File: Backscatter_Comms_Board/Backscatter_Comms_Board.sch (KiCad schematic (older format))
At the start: 49 parts, among them J1 SPK_IN, J2 Conn_01x09, J3 Conn_01x02, M1 BF1101WR, M2 BF1101WR, T1 SP-48, U1 ADG919BRMZ, U2 ADG841YKSZ-REEL7, U3 NCS2200SQ2T2G

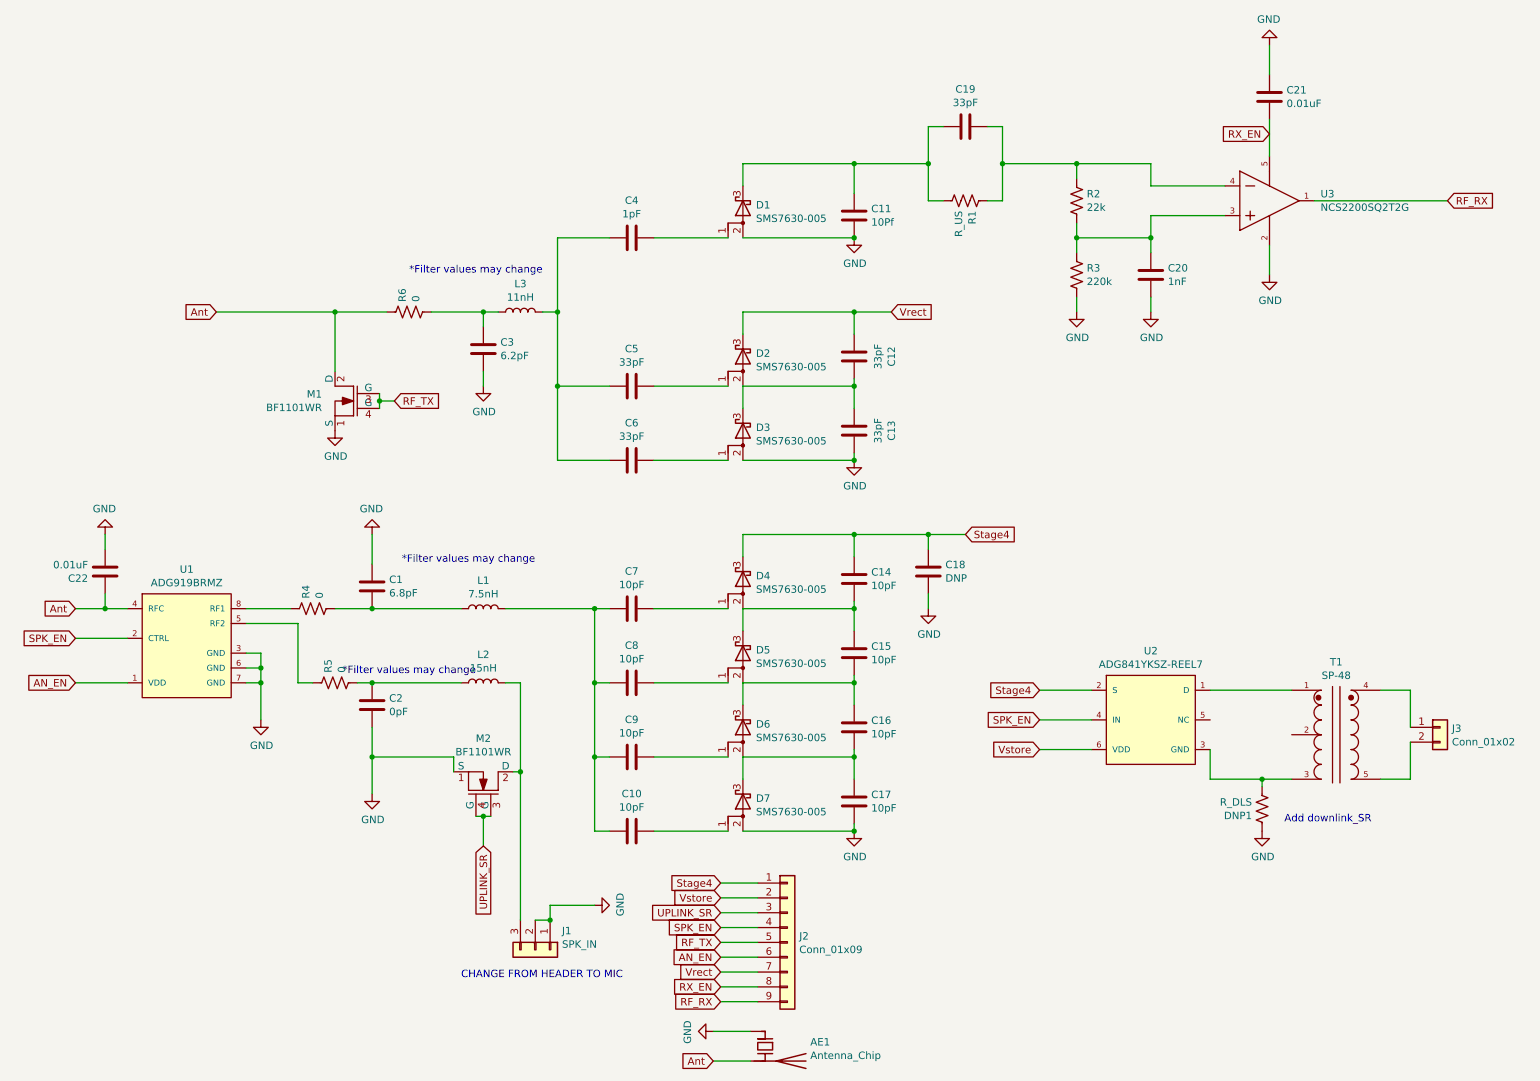
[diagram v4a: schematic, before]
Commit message: Small fixes final
fixed nmos enclosure(again) and added better text
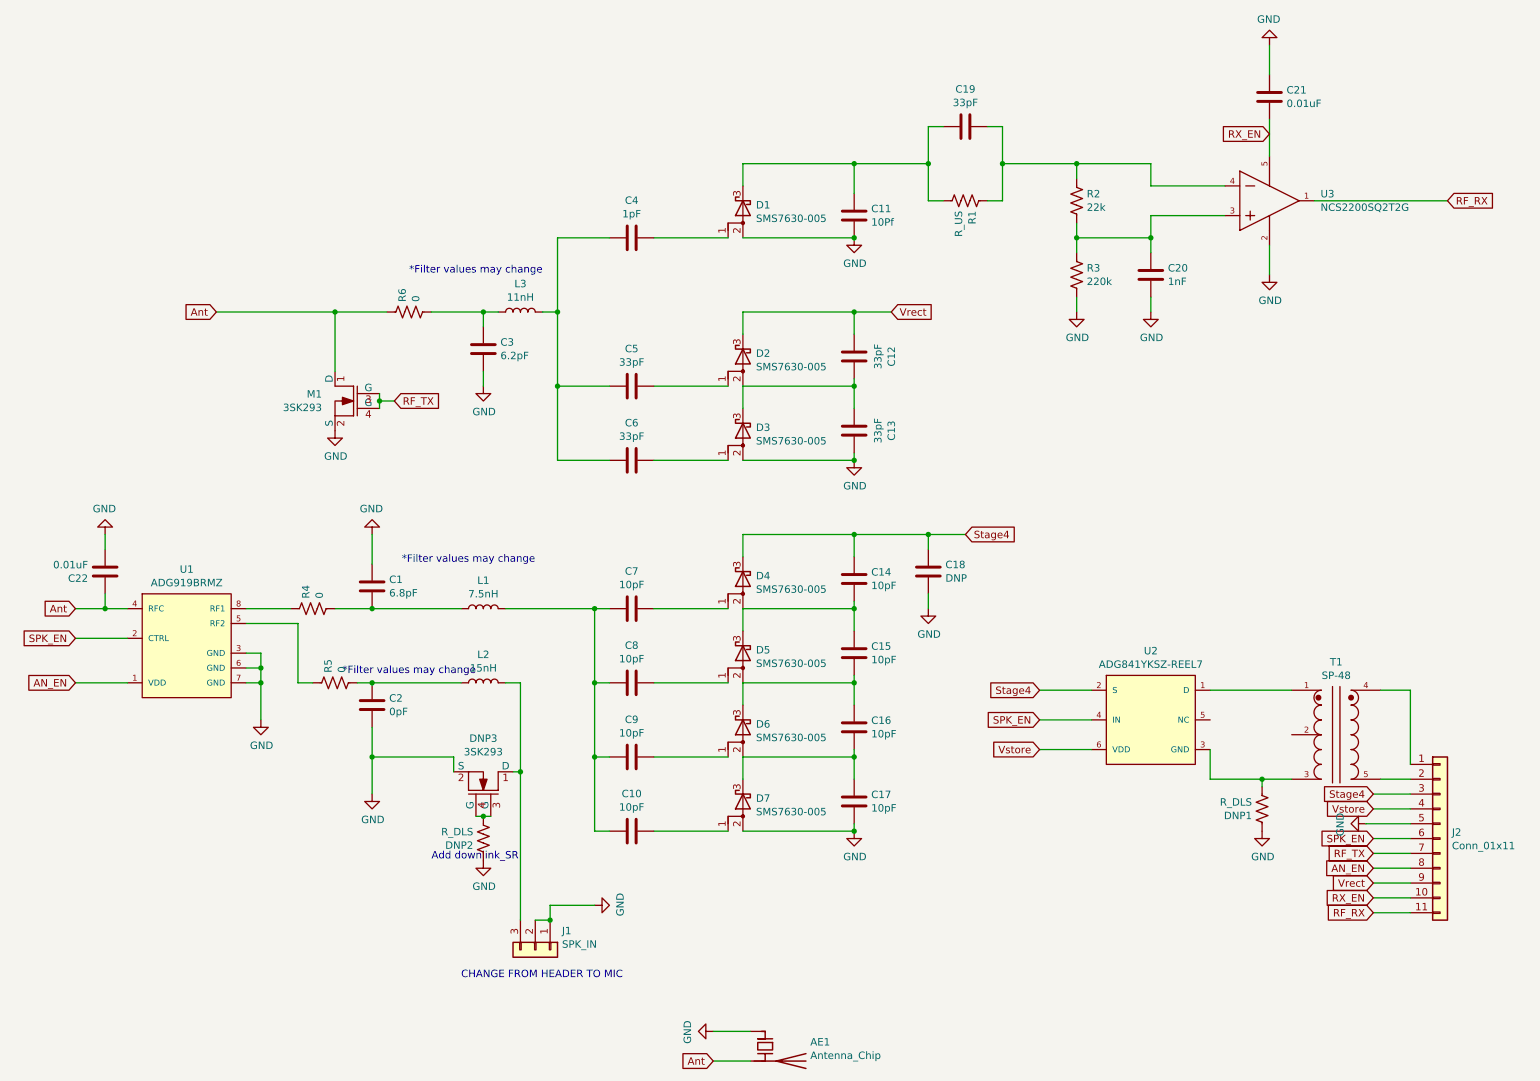
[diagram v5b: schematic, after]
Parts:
- removed J2: Conn_01x09, Connector_PinHeader_2.54mm:PinHeader_1x09_P2.54mm_Vertical, symbol Connector_Generic:Conn_01x09
- removed J3: Conn_01x02, Connector_PinHeader_2.54mm:PinHeader_1x02_P2.54mm_Vertical, symbol Connector_Generic:Conn_01x02
- removed M1, M2: BF1101WR, Local Components:BF1101WR, symbol ADG919:BF1101WR
- added DNP2: R_DLS, Resistor_SMD:R_0402_1005Metric_Pad0.72x0.64mm_HandSolder, symbol Device:R_US
- added DNP3, M1: 3SK293, Local Components:3SK293, symbol ADG919:3SK293
- added J2: Conn_01x11, Connector_PinHeader_2.54mm:PinHeader_1x11_P2.54mm_Vertical, symbol Connector_Generic:Conn_01x11
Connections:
- net AN_EN: now also J2.8 (Pin_8)
- net Ant: now also M1.1 (D)
- net GND: now also DNP2.1, DNP3.2 (S), J2.5 (Pin_5), M1.2 (S)
- net RF_RX: now also J2.11 (Pin_11)
- net RF_TX: now also J2.7 (Pin_7), M1.3 (G), M1.4 (G)
- net RX_EN: now also J2.10 (Pin_10)
- net SPK_EN: now also J2.6 (Pin_6)
- net Stage4: now also J2.3 (Pin_3)
- net Vrect: now also J2.9 (Pin_9)
- net Vstore: now also J2.4 (Pin_4)
- net at J1.3 (Pin_3), L2.2: now also DNP3.1 (D)
- net at T1.4: now also J2.1 (Pin_1)
- net at T1.5: now also J2.2 (Pin_2)
- new net: DNP2.2, DNP3.3 (G), DNP3.4 (G)
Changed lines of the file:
@@
 Wire Wire Line
 	3500 5000 4100 5000
-Wire Wire Line
-	4250 5900 4250 6100
 $Comp
 L Device:C C8
@@
 Text GLabel 10750 1750 2    50   Input ~ 0
 RF_RX
-Text GLabel 4250 6100 3    50   Input ~ 0
-UPLINK_SR
 Connection ~ 6750 3500
 $Comp
@@
 $EndComp
 Wire Wire Line
-	6100 6350 5850 6350
-Wire Wire Line
-	6100 6950 5850 6950
-Wire Wire Line
-	6100 7150 5850 7150
-Wire Wire Line
-	6100 6550 5850 6550
-Text GLabel 5850 6350 0    50   Input ~ 0
+	10500 5750 10250 5750
+Wire Wire Line
+	10500 6350 10250 6350
+Wire Wire Line
+	10500 6550 10250 6550
+Text GLabel 10250 5750 0    50   Input ~ 0
 Stage4
-Text GLabel 5850 7150 0    50   Input ~ 0
+Text GLabel 10250 6550 0    50   Input ~ 0
 RF_RX
 Text GLabel 7500 4000 2    50   Input ~ 0
@@
 Wire Wire Line
 	6750 2500 7000 2500
-Text GLabel 5850 6850 0    50   Input ~ 0
+Text GLabel 10250 6250 0    50   Input ~ 0
 AN_EN
 Text GLabel 5800 7550 0    50   Input ~ 0
@@
 	10300 5650 10500 5650
 $Comp
-L Connector_Generic:Conn_01x02 J3
-U 1 1 6103D8DC
-P 10700 5300
-F 0 "J3" H 10780 5292 50  0000 L CNN
-F 1 "Conn_01x02" H 10780 5201 50  0000 L CNN
-F 2 "Connector_PinHeader_2.54mm:PinHeader_1x02_P2.54mm_Vertical" H 10700 5300 50  0001 C CNN
-F 3 "~" H 10700 5300 50  0001 C CNN
-	1    10700 5300
-	1    0    0    -1
-$EndComp
-Wire Wire Line
-	10300 5050 10500 5050
-Wire Wire Line
-	10500 5050 10500 5300
-Wire Wire Line
-	10500 5400 10500 5650
-$Comp
 L power:GND #PWR09
 U 1 1 610492B0
@@
 $EndComp
 Connection ~ 6750 6000
-Text GLabel 5850 6550 0    50   Input ~ 0
-UPLINK_SR
 $Comp
 L power:GND #PWR013
@@
 	1    0    0    -1
 $EndComp
-Text GLabel 5850 6950 0    50   Input ~ 0
+Text GLabel 10250 6350 0    50   Input ~ 0
 Vrect
 $Comp
@@
 	-1   0    0    1
 $EndComp
-Text GLabel 5850 6750 0    50   Input ~ 0
+Text GLabel 10250 6150 0    50   Input ~ 0
 RF_TX
 Text GLabel 9550 1300 0    50   Input ~ 0
@@
 Wire Wire Line
 	1700 4500 1500 4500
-Text GLabel 5850 6450 0    50   Input ~ 0
+Text GLabel 10250 5850 0    50   Input ~ 0
 Vstore
 Wire Wire Line
-	5850 6450 6100 6450
-$Comp
-L Connector_Generic:Conn_01x09 J2
-U 1 1 60F82694
-P 6300 6750
-F 0 "J2" H 6380 6792 50  0000 L CNN
-F 1 "Conn_01x09" H 6380 6701 50  0000 L CNN
-F 2 "Connector_PinHeader_2.54mm:PinHeader_1x09_P2.54mm_Vertical" H 6300 6750 50  0001 C CNN
-F 3 "~" H 6300 6750 50  0001 C CNN
-	1    6300 6750
-	1    0    0    -1
-$EndComp
+	10250 5850 10500 5850
 $Comp
 L Device:R_US R6
@@
 Wire Wire Line
 	3100 5000 3000 5000
-Text Notes 9650 5950 0    50   ~ 0
-Add downlink_SR\n
-Wire Wire Line
-	6100 6650 5850 6650
-Text GLabel 5850 6650 0    50   Input ~ 0
+Wire Wire Line
+	10500 6050 10250 6050
+Text GLabel 10250 6050 0    50   Input ~ 0
 SPK_EN
 Wire Wire Line
-	5850 7050 6100 7050
-Text GLabel 5850 7050 0    50   Input ~ 0
+	10250 6450 10500 6450
+Text GLabel 10250 6450 0    50   Input ~ 0
 RX_EN
-$Comp
-L ADG919:BF1101WR M1
-U 1 1 6104D965
-P 3350 3100
-F 0 "M1" H 3538 3146 50  0000 L CNN
-F 1 "BF1101WR" H 3538 3055 50  0000 L CNN
-F 2 "Local Components:BF1101WR" H 3325 3100 50  0001 C CNN
-F 3 "~" H 3325 3100 50  0001 C CNN
-	1    3350 3100
-	-1   0    0    -1
-$EndComp
 $Comp
 L power:GND #PWR02
@@
 	3550 3100 3550 3150
 Connection ~ 3550 3100
-$Comp
-L ADG919:BF1101WR M2
-U 1 1 6107F5AB
-P 4250 5700
-F 0 "M2" V 4575 5700 50  0000 C CNN
-F 1 "BF1101WR" V 4484 5700 50  0000 C CNN
-F 2 "Local Components:BF1101WR" H 4225 5700 50  0001 C CNN
-F 3 "~" H 4225 5700 50  0001 C CNN
-	1    4250 5700
-	0    1    -1   0
-$EndComp
-Wire Wire Line
-	4300 5900 4250 5900
-Connection ~ 4250 5900
-Wire Wire Line
-	4250 5900 4200 5900
-Wire Wire Line
-	6100 6750 5850 6750
-Wire Wire Line
-	5850 6850 6100 6850
+Wire Wire Line
+	10500 6150 10250 6150
+Wire Wire Line
+	10250 6250 10500 6250
 Wire Wire Line
 	9150 5650 9500 5650
@@
 Wire Wire Line
 	9500 5650 9700 5650
+$Comp
+L power:GND #PWR0103
+U 1 1 61191A72
+P 4250 6200
+F 0 "#PWR0103" H 4250 5950 50  0001 C CNN
+F 1 "GND" H 4255 6027 50  0000 C CNN
+F 2 "" H 4250 6200 50  0001 C CNN
+F 3 "" H 4250 6200 50  0001 C CNN
+	1    4250 6200
+	1    0    0    -1
+$EndComp
+Text Notes 3900 6200 0    50   ~ 0
+Add downlink_SR\n
+$Comp
+L Device:R_US DNP2
+U 1 1 61191A79
+P 4250 6050
+F 0 "DNP2" H 4318 6096 50  0000 L CNN
+F 1 "R_DLS" H 4318 6005 50  0000 L CNN
+F 2 "Resistor_SMD:R_0402_1005Metric_Pad0.72x0.64mm_HandSolder" V 4290 6040 50  0001 C CNN
+F 3 "~" H 4250 6050 50  0001 C CNN
+	1    4250 6050
+	-1   0    0    1
+$EndComp
+Wire Wire Line
+	4200 5900 4250 5900
+Connection ~ 4250 5900
+Wire Wire Line
+	4250 5900 4300 5900
+$Comp
+L ADG919:3SK293 M1
+U 1 1 611C441C
+P 3350 3100
+F 0 "M1" H 3538 3146 50  0000 L CNN
+F 1 "3SK293" H 3538 3055 50  0000 L CNN
+F 2 "Local Components:3SK293" H 3325 3100 50  0001 C CNN
+F 3 "~" H 3325 3100 50  0001 C CNN
+	1    3350 3100
+	-1   0    0    -1
+$EndComp
+$Comp
+L ADG919:3SK293 DNP3
+U 1 1 611D3BD0
+P 4250 5700
+F 0 "DNP3" V 4575 5700 50  0000 C CNN
+F 1 "3SK293" V 4484 5700 50  0000 C CNN
+F 2 "Local Components:3SK293" H 4225 5700 50  0001 C CNN
+F 3 "~" H 4225 5700 50  0001 C CNN
+	1    4250 5700
+	0    1    -1   0
+$EndComp
+$Comp
+L power:GND #PWR0104
+U 1 1 611E9FE5
+P 10200 5950
+F 0 "#PWR0104" H 10200 5700 50  0001 C CNN
+F 1 "GND" H 10205 5777 50  0000 C CNN
+F 2 "" H 10200 5950 50  0001 C CNN
+F 3 "" H 10200 5950 50  0001 C CNN
+	1    10200 5950
+	0    1    1    0
+$EndComp
+Wire Wire Line
+	10500 5950 10200 5950
+$Comp
+L Connector_Generic:Conn_01x11 J2
+U 1 1 61200553
+P 10700 6050
+F 0 "J2" H 10780 6092 50  0000 L CNN
+F 1 "Conn_01x11" H 10780 6001 50  0000 L CNN
+F 2 "Connector_PinHeader_2.54mm:PinHeader_1x11_P2.54mm_Vertical" H 10700 6050 50  0001 C CNN
+F 3 "~" H 10700 6050 50  0001 C CNN
+	1    10700 6050
+	1    0    0    -1
+$EndComp
+Wire Wire Line
+	10300 5050 10500 5050
+Wire Wire Line
+	10500 5050 10500 5550
 $EndSCHEMATC

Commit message: Final v1 backscatter board
Sending to oshpark right after I push!
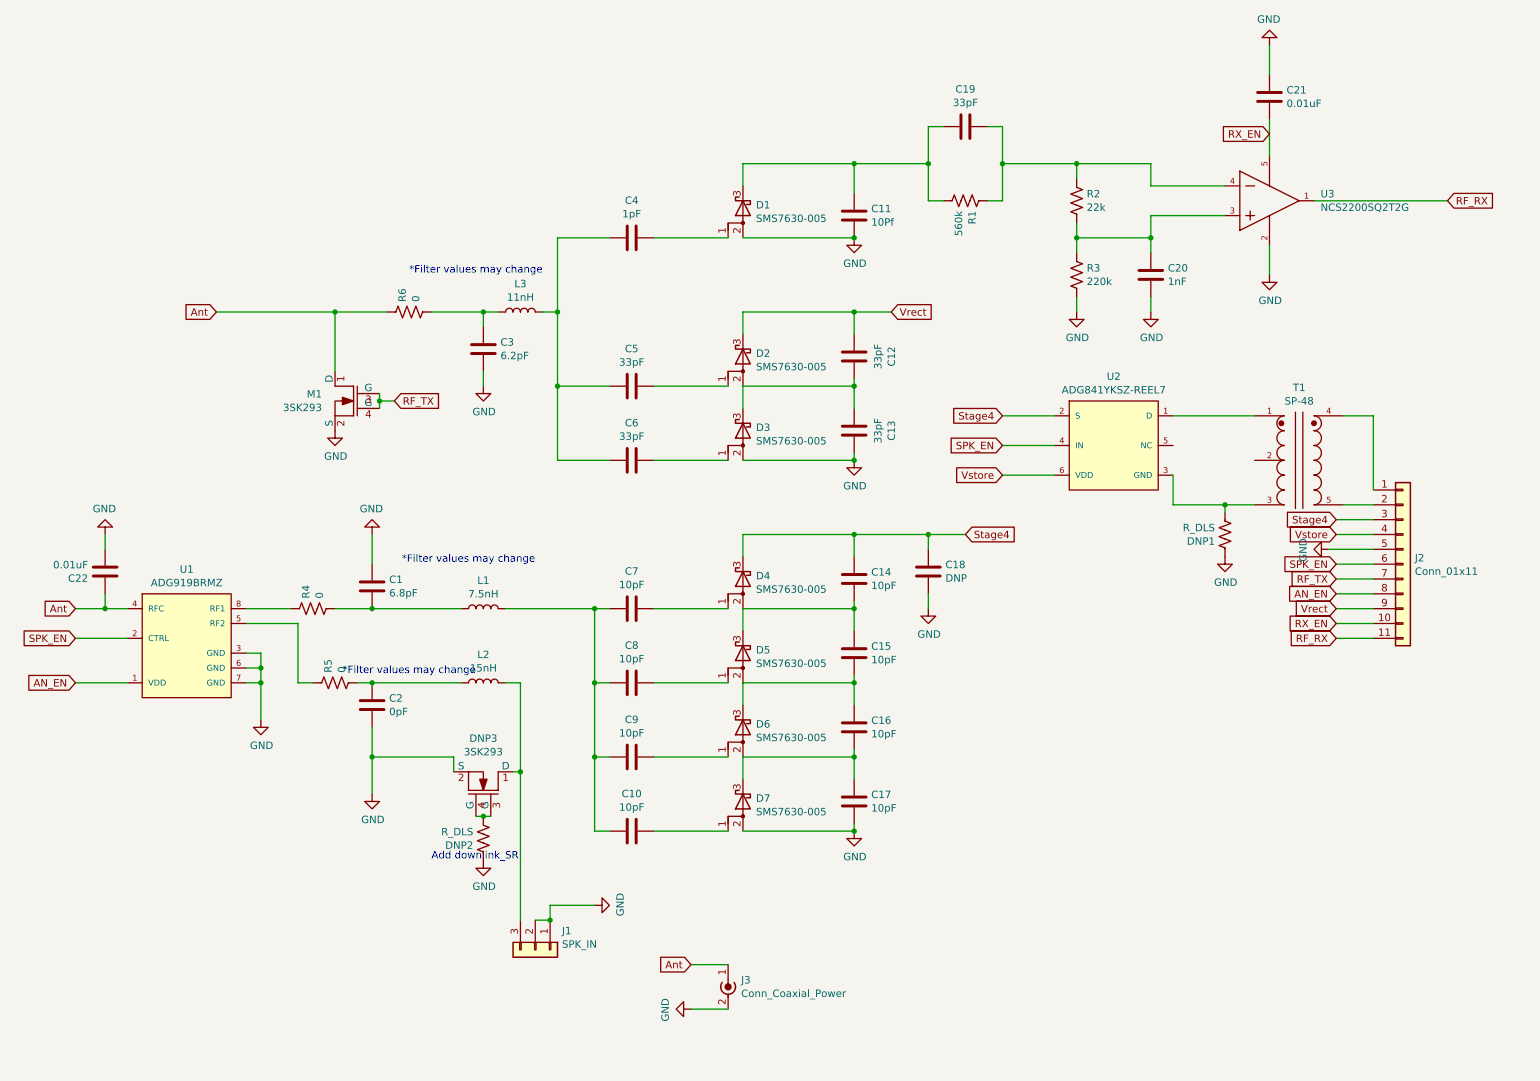
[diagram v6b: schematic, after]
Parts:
- removed AE1: Antenna_Chip, Connector_Coaxial:MMCX_Molex_73415-0961_Horizontal_0.8mm-PCB, symbol Device:Antenna_Chip
- added J3: Conn_Coaxial_Power, Connector_Coaxial:MMCX_Molex_73415-0961_Horizontal_0.8mm-PCB, symbol Connector:Conn_Coaxial_Power
- R1: value R_US -> 560k
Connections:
- net Ant: now also J3.1 (In)
- net GND: now also J3.2 (Ext)
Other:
- note removed: "CHANGE FROM HEADER TO MIC"
- moved on the sheet: DNP1, J2, T1, U2

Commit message: trying to make commit workj >:(
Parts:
- removed C1: 6.8pF, Capacitor_SMD:C_0402_1005Metric_Pad0.74x0.62mm_HandSolder, symbol Device:C
- removed C10, C14, C15, C16, C17, C7, C8, C9: 10pF, Capacitor_SMD:C_0402_1005Metric_Pad0.74x0.62mm_HandSolder, symbol Device:C
- removed C11: 10Pf, Capacitor_SMD:C_0402_1005Metric_Pad0.74x0.62mm_HandSolder, symbol Device:C
- removed C12, C13, C19, C5, C6: 33pF, Capacitor_SMD:C_0402_1005Metric_Pad0.74x0.62mm_HandSolder, symbol Device:C
- removed C18: DNP, Capacitor_SMD:C_0402_1005Metric_Pad0.74x0.62mm_HandSolder, symbol Device:C
- removed C2: 0pF, Capacitor_SMD:C_0402_1005Metric_Pad0.74x0.62mm_HandSolder, symbol Device:C
- removed C20: 1nF, Capacitor_SMD:C_0402_1005Metric_Pad0.74x0.62mm_HandSolder, symbol Device:C
- removed C21, C22: 0.01uF, Capacitor_SMD:C_0402_1005Metric_Pad0.74x0.62mm_HandSolder, symbol Device:C
- removed C3: 6.2pF, Capacitor_SMD:C_0402_1005Metric_Pad0.74x0.62mm_HandSolder, symbol Device:C
- removed C4: 1pF, Capacitor_SMD:C_0402_1005Metric_Pad0.74x0.62mm_HandSolder, symbol Device:C
- removed D1, D2, D3, D4, D5, D6, D7: SMS7630-005, Local Components:SOT95P237X112-3N, symbol Device:D_Schottky_AAK
- removed DNP1, DNP2: R_DLS, Resistor_SMD:R_0402_1005Metric_Pad0.72x0.64mm_HandSolder, symbol Device:R_US
- removed DNP3, M1: 3SK293, Local Components:3SK293, symbol ADG919:3SK293
- removed J1: SPK_IN, Local Components:Multi-purpose_mic, symbol Connector_Generic:Conn_01x03
- removed J2: Conn_01x11, Connector_PinHeader_2.54mm:PinHeader_1x11_P2.54mm_Vertical, symbol Connector_Generic:Conn_01x11
- removed J3: Conn_Coaxial_Power, Connector_Coaxial:MMCX_Molex_73415-0961_Horizontal_0.8mm-PCB, symbol Connector:Conn_Coaxial_Power
- removed L1: 7.5nH, Inductor_SMD:L_0402_1005Metric, symbol Device:L
- removed L2: 15nH, Inductor_SMD:L_0402_1005Metric, symbol Device:L
- removed L3: 11nH, Inductor_SMD:L_0402_1005Metric, symbol Device:L
- removed R1: 560k, Resistor_SMD:R_0402_1005Metric_Pad0.72x0.64mm_HandSolder, symbol Device:R_US
- removed R2: 22k, Resistor_SMD:R_0402_1005Metric_Pad0.72x0.64mm_HandSolder, symbol Device:R_US
- removed R3: 220k, Resistor_SMD:R_0402_1005Metric_Pad0.72x0.64mm_HandSolder, symbol Device:R_US
- removed R4, R5, R6: 0, Resistor_SMD:R_0402_1005Metric_Pad0.72x0.64mm_HandSolder, symbol Device:R_US
- removed T1: SP-48, Local Components:XFMR_SP-48, symbol SP-48:SP-48
- removed U1: ADG919BRMZ, Local Components:Analog_Devices-ADG919BRMZ-Level_C, symbol ADG919:ADG919BRMZ
- removed U2: ADG841YKSZ-REEL7, Local Components:Analog_Devices-ADG841YKSZ-REEL7-Level_C, symbol ADG841:ADG841YKSZ-REEL7
- removed U3: NCS2200SQ2T2G, Local Components:On_Semiconductor-NCS2200SQ2T2G-Manufacturer_Recommended, symbol A_Comparator:NCS2200SQ2T2G
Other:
- note removed: "*Filter values may change\n"
- note removed: "Add downlink_SR\n"
